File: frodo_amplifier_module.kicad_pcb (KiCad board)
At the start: 2 copper layers, 16.5 x 21.2 mm, 23 parts, among them IC1 INA826AID, IC2 AS321KTR-G1, J1 Conn_01x01_Socket, J2 Conn_01x01_Socket, J3 Conn_01x01_Socket, J4 Conn_01x01_Socket, J5 Conn_01x01_Socket, J6 Conn_01x01_Socket, J7 Conn_01x01_Socket, J8 Conn_01x01_Socket

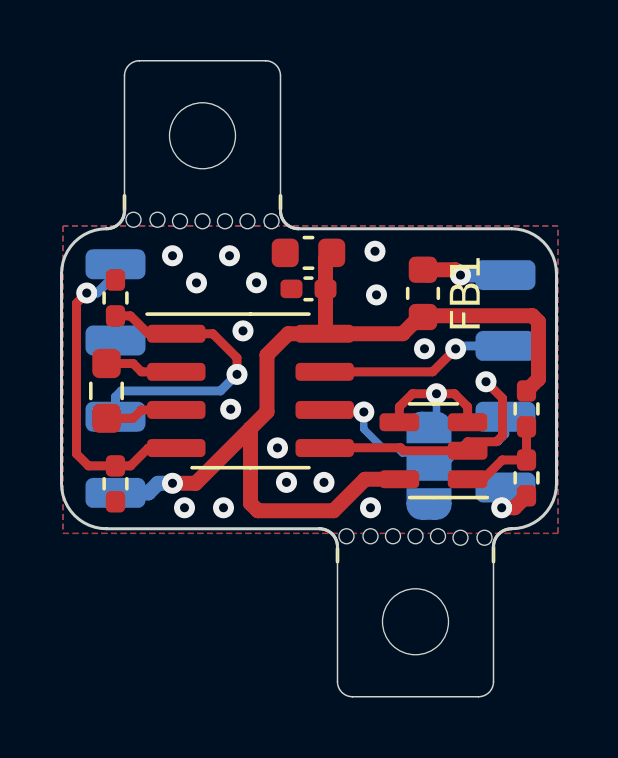
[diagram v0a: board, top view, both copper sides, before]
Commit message: changed folder layout, optimised gnd routing
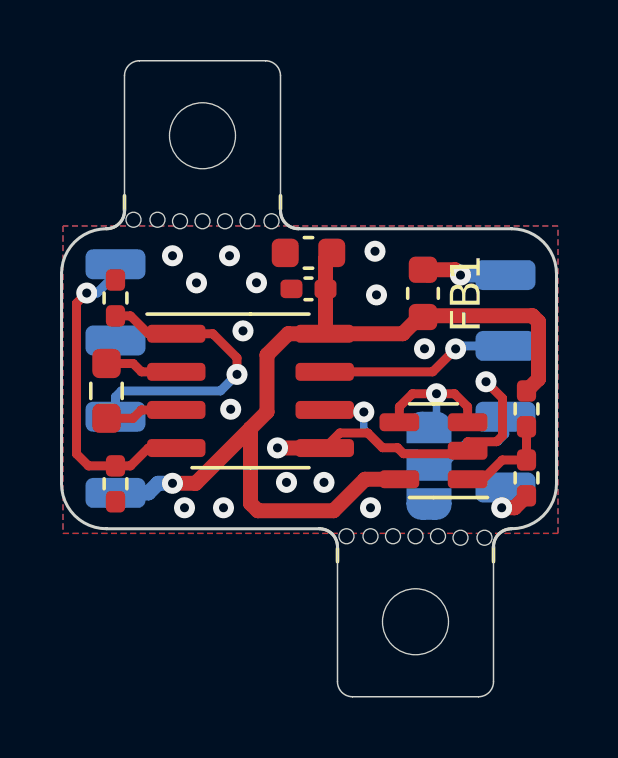
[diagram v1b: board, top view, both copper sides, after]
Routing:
- net GND: track 9.37 -> 11.4 mm
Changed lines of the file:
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@@
   (segment (start 86.5375 53.1) (end 87.5 53.1) (width 0.3) (layer "F.Cu") (net 2))
   (segment (start 87.7 51.65) (end 87.15 51.1) (width 0.3) (layer "F.Cu") (net 2))
-  (segment (start 84.3 53.3) (end 84.4 53.4) (width 0.3) (layer "F.Cu") (net 2))
+  (segment (start 84.2 53.3) (end 84.4 53.5) (width 0.3) (layer "F.Cu") (net 2))
+  (segment (start 84.4 53.5) (end 86.4375 53.5) (width 0.3) (layer "F.Cu") (net 2))
+  (segment (start 83.207832 52.807832) (end 83.7 53.3) (width 0.3) (layer "F.Cu") (net 2))
+  (segment (start 86.4375 53.5) (end 86.5375 53.4) (width 0.3) (layer "F.Cu") (net 2))
+  (segment (start 80.205 53.31) (end 80.2 53.305) (width 0.3) (layer "F.Cu") (net 2))
+  (segment (start 81.775 53.31) (end 80.205 53.31) (width 0.5) (layer "F.Cu") (net 2))
   (segment (start 87.673661 55.3005) (end 88.102 55.3005) (width 0.5) (layer "F.Cu") (net 2))
-  (segment (start 81.775 53.31) (end 81.785 53.3) (width 0.3) (layer "F.Cu") (net 2))
+  (segment (start 81.775 53.31) (end 82.277168 52.807832) (width 0.3) (layer "F.Cu") (net 2))
   (segment (start 86.5375 53.4) (end 86.5375 53.1) (width 0.3) (layer "F.Cu") (net 2))
-  (segment (start 81.785 53.3) (end 84.3 53.3) (width 0.3) (layer "F.Cu") (net 2))
-  (segment (start 84.4 53.4) (end 86.5375 53.4) (width 0.3) (layer "F.Cu") (net 2))
+  (segment (start 82.277168 52.807832) (end 83.207832 52.807832) (width 0.3) (layer "F.Cu") (net 2))
   (segment (start 87.7 52.9) (end 87.7 51.65) (width 0.3) (layer "F.Cu") (net 2))
   (segment (start 88.102 55.3005) (end 88.5 54.9025) (width 0.5) (layer "F.Cu") (net 2))
   (segment (start 87.5 53.1) (end 87.7 52.9) (width 0.3) (layer "F.Cu") (net 2))
+  (segment (start 83.7 53.3) (end 84.2 53.3) (width 0.3) (layer "F.Cu") (net 2))
   (via (at 80.5 54.455) (size 0.7) (drill 0.3) (layers "F.Cu" "B.Cu") (free) (net 2))
   (via (at 78.639708 52.016474) (size 0.7) (drill 0.3) (layers "F.Cu" "B.Cu") (free) (net 2))

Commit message: added silcscrean for better usability
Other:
- board text added: "<io sens>"
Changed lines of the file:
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@@
     (effects (font (size 1 1) (thickness 0.153)) (justify left bottom mirror))
+  )
+  (gr_text "<io       sens>" (at 73.3 51.5) (layer "B.SilkS")
+    (effects (font (size 1 1) (thickness 0.15)) (justify right bottom mirror))
   )
   (gr_text "o+" (at 88.7 49.2) (layer "B.SilkS")
